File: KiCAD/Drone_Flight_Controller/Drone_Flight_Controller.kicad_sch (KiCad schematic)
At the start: 0 parts

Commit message: Revision 3
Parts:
- added FID1, FID2: Fiducial, Fiducial:Fiducial_0.5mm_Mask1mm, symbol Mechanical:Fiducial
- added G3: Logo_HTL_Steyr_Small, Symbol_:HTL-Steyr-Logo_5mm_Copper, symbol Graphic_:Logo_HTL_Steyr_Small
- added SYM1: Logo_Open_Hardware_Small, Symbol:OSHW-Logo2_9.8x8mm_SilkScreen, symbol Graphic:Logo_Open_Hardware_Small
- added SYM2: KiCad-Logo, Symbol:KiCad-Logo2_6mm_SilkScreen, symbol Graphic:Logo_Open_Hardware_Small
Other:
- added sheet Core (Core.kicad_sch)
- added sheet Peripherals (Peripherals.kicad_sch)

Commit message: Re-annotate
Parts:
- renumbered FID2 to FID1, FID1 to FID2, G3 to G1
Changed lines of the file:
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@@
 		(dnp no)
 		(fields_autoplaced yes)
-		(property "Reference" "#FLG02"
+		(property "Reference" "#FLG01"
 			(at 246.38 43.815 0)
 			(effects
@@
 			(project "Drone_Flight_Controller"
 				(path "/51ab9491-7068-4b24-bb38-47a0c739796e"
-					(reference "#FLG02")
+					(reference "#FLG01")
 					(unit 1)
 				)
@@
 		(dnp no)
 		(fields_autoplaced yes)
-		(property "Reference" "FID2"
+		(property "Reference" "FID1"
 			(at 251.46 106.045 0)
 			(effects
@@
 			(project "Drone_Flight_Controller"
 				(path "/51ab9491-7068-4b24-bb38-47a0c739796e"
-					(reference "FID2")
+					(reference "FID1")
 					(unit 1)
 				)
@@
 		(dnp no)
 		(fields_autoplaced yes)
-		(property "Reference" "FID1"
+		(property "Reference" "FID2"
 			(at 251.46 116.205 0)
 			(effects
@@
 			(project "Drone_Flight_Controller"
 				(path "/51ab9491-7068-4b24-bb38-47a0c739796e"
-					(reference "FID1")
+					(reference "FID2")
 					(unit 1)
 				)
@@
 		(dnp no)
 		(fields_autoplaced yes)
-		(property "Reference" "#PWR011"
+		(property "Reference" "#PWR02"
 			(at 259.08 48.26 0)
 			(effects
@@
 			(project "Drone_Flight_Controller"
 				(path "/51ab9491-7068-4b24-bb38-47a0c739796e"
-					(reference "#PWR011")
+					(reference "#PWR02")
 					(unit 1)
 				)
@@
 		(dnp no)
 		(fields_autoplaced yes)
-		(property "Reference" "G3"
+		(property "Reference" "G1"
 			(at 252.73 55.4086 0)
 			(effects
@@
 			(project "Drone_Flight_Controller"
 				(path "/51ab9491-7068-4b24-bb38-47a0c739796e"
-					(reference "G3")
+					(reference "G1")
 					(unit 1)
 				)
@@
 		(dnp no)
 		(fields_autoplaced yes)
-		(property "Reference" "#FLG01"
+		(property "Reference" "#FLG02"
 			(at 259.08 37.465 0)
 			(effects
@@
 			(project "Drone_Flight_Controller"
 				(path "/51ab9491-7068-4b24-bb38-47a0c739796e"
-					(reference "#FLG01")
+					(reference "#FLG02")
 					(unit 1)
 				)
@@
 		(on_board yes)
 		(dnp no)
-		(property "Reference" "#PWR010"
+		(property "Reference" "#PWR01"
 			(at 246.38 43.18 0)
 			(effects
@@
 			(project ""
 				(path "/51ab9491-7068-4b24-bb38-47a0c739796e"
-					(reference "#PWR010")
-					(unit 1)
-				)
+					(reference "#PWR01")
+					(unit 1)
+				)

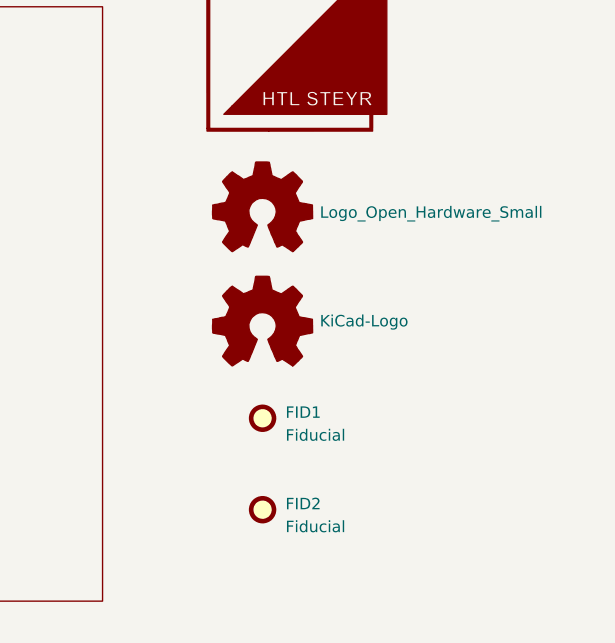
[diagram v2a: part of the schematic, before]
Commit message: Implement feedback from Prof. Parzer
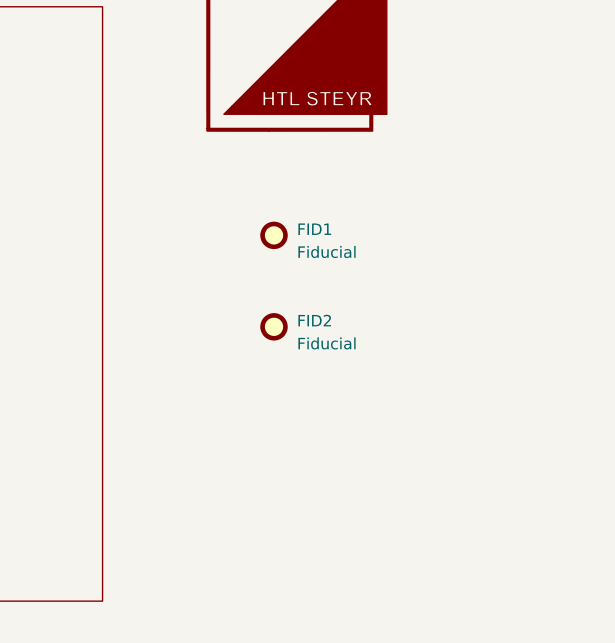
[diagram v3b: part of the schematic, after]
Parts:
- removed SYM1: Logo_Open_Hardware_Small, Symbol:OSHW-Logo2_9.8x8mm_SilkScreen, symbol Graphic:Logo_Open_Hardware_Small
- removed SYM2: KiCad-Logo, Symbol:KiCad-Logo2_6mm_SilkScreen, symbol Graphic:Logo_Open_Hardware_Small
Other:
- moved on the sheet: FID1, FID2
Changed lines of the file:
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@@
 	(symbol
 		(lib_id "Mechanical:Fiducial")
-		(at 248.92 106.68 0)
-		(unit 1)
-		(exclude_from_sim yes)
+		(at 250.19 86.36 0)
+		(unit 1)
+		(exclude_from_sim no)
 		(in_bom no)
 		(on_board yes)
@@
 		(fields_autoplaced yes)
 		(property "Reference" "FID1"
-			(at 251.46 106.045 0)
+			(at 252.73 85.725 0)
 			(effects
 				(font
@@
 		)
 		(property "Value" "Fiducial"
-			(at 251.46 108.585 0)
+			(at 252.73 88.265 0)
 			(effects
 				(font
@@
 		)
 		(property "Footprint" "Fiducial:Fiducial_0.5mm_Mask1mm"
-			(at 248.92 106.68 0)
+			(at 250.19 86.36 0)
 			(effects
 				(font
@@
 		)
 		(property "Datasheet" "~"
-			(at 248.92 106.68 0)
+			(at 250.19 86.36 0)
 			(effects
 				(font
@@
 		)
 		(property "Description" "Fiducial Marker"
-			(at 248.92 106.68 0)
+			(at 250.19 86.36 0)
 			(effects
 				(font
@@
 	(symbol
 		(lib_id "Mechanical:Fiducial")
-		(at 248.92 116.84 0)
-		(unit 1)
-		(exclude_from_sim yes)
+		(at 250.19 96.52 0)
+		(unit 1)
+		(exclude_from_sim no)
 		(in_bom no)
 		(on_board yes)
@@
 		(fields_autoplaced yes)
 		(property "Reference" "FID2"
-			(at 251.46 116.205 0)
+			(at 252.73 95.885 0)
 			(effects
 				(font
@@
 		)
 		(property "Value" "Fiducial"
-			(at 251.46 118.745 0)
+			(at 252.73 98.425 0)
 			(effects
 				(font
@@
 		)
 		(property "Footprint" "Fiducial:Fiducial_0.5mm_Mask1mm"
-			(at 248.92 116.84 0)
+			(at 250.19 96.52 0)
 			(effects
 				(font
@@
 		)
 		(property "Datasheet" "~"
-			(at 248.92 116.84 0)
+			(at 250.19 96.52 0)
 			(effects
 				(font
@@
 		)
 		(property "Description" "Fiducial Marker"
-			(at 248.92 116.84 0)
+			(at 250.19 96.52 0)
 			(effects
 				(font
@@
 		(at 252.73 64.77 0)
 		(unit 1)
-		(exclude_from_sim yes)
+		(exclude_from_sim no)
 		(in_bom no)
 		(on_board yes)
@@
 	)
 	(symbol
-		(lib_id "Graphic:Logo_Open_Hardware_Small")
-		(at 248.92 96.52 0)
-		(unit 1)
-		(exclude_from_sim yes)
-		(in_bom no)
-		(on_board yes)
-		(dnp no)
-		(fields_autoplaced yes)
-		(property "Reference" "SYM2"
-			(at 248.92 89.535 0)
-			(effects
-				(font
-					(size 1.27 1.27)
-				)
-				(hide yes)
-			)
-		)
-		(property "Value" "KiCad-Logo"
-			(at 255.27 95.885 0)
-			(effects
-				(font
-					(size 1.27 1.27)
-				)
-				(justify left)
-			)
-		)
-		(property "Footprint" "Symbol:KiCad-Logo2_6mm_SilkScreen"
-			(at 248.92 96.52 0)
-			(effects
-				(font
-					(size 1.27 1.27)
-				)
-				(hide yes)
-			)
-		)
-		(property "Datasheet" "~"
-			(at 248.92 96.52 0)
-			(effects
-				(font
-					(size 1.27 1.27)
-				)
-				(hide yes)
-			)
-		)
-		(property "Description" "Open Hardware logo, small"
-			(at 248.92 96.52 0)
-			(effects
-				(font
-					(size 1.27 1.27)
-				)
-				(hide yes)
-			)
-		)
-		(instances
-			(project "Drone_Flight_Controller"
-				(path "/51ab9491-7068-4b24-bb38-47a0c739796e"
-					(reference "SYM2")
-					(unit 1)
-				)
-			)
-		)
-	)
-	(symbol
 		(lib_id "power:PWR_FLAG")
 		(at 259.08 39.37 0)
@@
 					(unit 1)
 				)
-			)
-		)
-	)
-	(symbol
-		(lib_id "Graphic:Logo_Open_Hardware_Small")
-		(at 248.92 83.82 0)
-		(unit 1)
-		(exclude_from_sim yes)
-		(in_bom no)
-		(on_board yes)
-		(dnp no)
-		(fields_autoplaced yes)
-		(property "Reference" "SYM1"
-			(at 248.92 76.835 0)
-			(effects
-				(font
-					(size 1.27 1.27)
-				)
-				(hide yes)
-			)
-		)
-		(property "Value" "Logo_Open_Hardware_Small"
-			(at 255.27 83.82 0)
-			(effects
-				(font
-					(size 1.27 1.27)
-				)
-				(justify left)
-			)
-		)
-		(property "Footprint" "Symbol:OSHW-Logo2_9.8x8mm_SilkScreen"
-			(at 248.92 83.82 0)
-			(effects
-				(font
-					(size 1.27 1.27)
-				)
-				(hide yes)
-			)
-		)
-		(property "Datasheet" "~"
-			(at 248.92 83.82 0)
-			(effects
-				(font
-					(size 1.27 1.27)
-				)
-				(hide yes)
-			)
-		)
-		(property "Description" "Open Hardware logo, small"
-			(at 248.92 83.82 0)
-			(effects
-				(font
-					(size 1.27 1.27)
-				)
-				(hide yes)
-			)
-		)
-		(instances
-			(project "Drone_Flight_Controller"
-				(path "/51ab9491-7068-4b24-bb38-47a0c739796e"
-					(reference "SYM1")
-					(unit 1)
-				)
